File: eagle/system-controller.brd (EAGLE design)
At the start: 99 x 100 mm, 227 parts, among them IC1 TS4100, Q0 MOSFET-P-N-PAIR, Q1 MOSFET-P-N-PAIR, Q10 DNP/NTR4101P, Q11 DNP/NTR4101P, Q12 DNP/NTR4101P, Q2 MOSFET-P-N-PAIR, Q3 MOSFET-P-N-PAIR, Q4 MOSFET-P-N-PAIR, Q5 MOSFET-P-N-PAIR, Q6 MOSFET-P-N-PAIR, Q7 MOSFET-P-N-PAIR, Q9 DNP/NTR4101P, SW0 TPS25944LRVCRWQFN-20-3X4, SW1 TPS25944LRVCRWQFN-20-3X4, SW2 TPS25944LRVCRWQFN-20-3X4, SW3 TPS25944LRVCRWQFN-20-3X4, SW4 TPS25944LRVCRWQFN-20-3X4, SW5 TPS25944LRVCRWQFN-20-3X4, SW6 TPS25944LRVCRWQFN-20-3X4, SW7 TPS25944LRVCRWQFN-20-3X4, U1 MEGA128-A, X1 8 MHz CRYSTAL-ABRACON-ABM3-SMD

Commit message: latetest changes pushed
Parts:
- removed CFUSE7, RHWWD0, RHWWD1, RHWWD2: TBD, rcl_custom:.0603-B-NOSILK
- removed CFUSE7A: 1uF, rcl_custom:.0603-B-NOSILK
- removed LED12: DNP/AMB, psas_c3_team05:LED-0603
- removed RA8: 47k, rcl_custom:.0603-B-NOSILK
- removed RHWWD3: 1k, rcl_custom:.0603-B-NOSILK
- added C19: TBD, rcl_custom:.0603-B-NOSILK
- added C20: 1uF, rcl_custom:.0603-B-NOSILK
- added LED8: DNP/AMB, psas_c3_team05:LED-0603
- added RA0: 47k, rcl_custom:.0603-B-NOSILK
- added RN1, RN2, RN3: 390, rcl_custom:.0603-B-NOSILK
- added RN4: 10k, rcl_custom:.0603-B-NOSILK
- added TP28, TP29, TP30, TP31, TP32, TP33, TP34, TP5: TEST-POINT, Tova:2MM-TEST-POINT
- CN1: value TBD -> 22u
- J1: value (none) -> 1
- Q13: value (none) -> DON3035L
- RILIM0, RILIM1, RILIM2, RILIM3, RILIM4, RILIM5, RILIM6, RILIM7: value TBD -> 47k
- RNR: value TBD -> 470k
- moved R2 110.7 mm to (92.5, 88.7), turned to 0 degrees
- moved R8 106.5 mm to (92.5, 79.0), turned to 0 degrees
- moved R14 103.0 mm to (92.5, 69.5), turned to 0 degrees
- moved R20 99.5 mm to (92.5, 59.5), turned to 0 degrees
- moved R61 92.9 mm to (69.0, 5.50)
- moved R6 89.3 mm to (45.0, 5.50)
- moved R28 88.8 mm to (92.5, 49.5)
- moved R24 85.0 mm to (72.0, 5.50)
- moved R33 79.2 mm to (92.5, 39.4), turned to 0 degrees
- moved R12 78.9 mm to (47.9, 5.50)
- moved R22 78.2 mm to (75.0, 5.50)
- moved R23 73.6 mm to (78.0, 5.52)
- moved R38 73.5 mm to (92.5, 29.0), turned to 0 degrees
- moved R43 69.7 mm to (92.6, 18.9), turned to 0 degrees
- moved R18 69.4 mm to (51.0, 5.50)
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- renumbered CHWWD to CN1, RHWWD4 to RNR
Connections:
- net VBC1 renamed VCB1
- net VBC2 renamed VCB2
- net VBC4 renamed VCB4
- net VBC5 renamed VCB5
- net VBC6 renamed VCB6
- net VBC7 renamed VCB7
- removed net GMD: LED0.K
- net 3V: now also RA0.1; no longer RA8.1
- net GND: now also C19.2, C20.1, LED0.K, LED8.K, RN4.2; no longer CFUSE7.2, CFUSE7A.1, LED12.K, RHWWD3.2
- net I2C-SCL: now also TP5.1
- net I2C-SDA: now also TP28.1
- net N$109: now also RN1.1, RN2.1, RN3.1, RN4.1; no longer RHWWD0.1, RHWWD1.1, RHWWD2.1, RHWWD3.1
- net N$50: now also R2.2
- net N$53: now also LED11.A; no longer LED12.A
- net N$56: now also LED10.A; no longer LED11.A
- net N$57: now also LED8.A; no longer LED9.A
- net N$60: now also LED9.A; no longer LED10.A
- net N$70: now also C19.1; no longer CFUSE7.1
- net NUCLEAROPTION0: now also RN3.2; no longer RHWWD2.2
- net NUCLEAROPTION1: now also RN2.2; no longer RHWWD1.2
- net NUCLEAROPTION2: now also RN1.2; no longer RHWWD0.2
- net UART_FC_RX: now also TP30.1
- net UART_FC_TX: now also TP31.1
- net UART_FC_VCC: now also TP29.1
- net UART_LGR_RX: now also TP33.1
- net UART_LGR_TX: now also TP34.1
- net UART_LGR_VCC: now also TP32.1
- net VBUS: now also C20.2; no longer CFUSE7A.2
- net VCB0_!FLT: now also RA0.2; no longer RA1.2
- net VCB1_!FLT: now also RA1.2; no longer RA2.2
- net VCB2_!FLT: now also RA2.2; no longer RA3.2
- net VCB3_!FLT: now also RA3.2; no longer RA4.2
- net VCB4_!FLT: now also RA4.2; no longer RA5.2
- net VCB5_!FLT: now also RA5.2; no longer RA6.2
- net VCB6_!FLT: now also RA6.2; no longer RA7.2
- net VCB7_!FLT: now also RA7.2; no longer RA8.2
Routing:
- net VCB0_EN: track 14.2 -> 164.1 mm, vias 0 -> 4
- net VCB2_EN: track 15.8 -> 163.1 mm, vias 0 -> 4
- net N$55: track 2.19 -> 148.4 mm, vias 0 -> 2
- net VCB1_EN: track 14.9 -> 154.9 mm, vias 0 -> 6
- net N$49: track 145.1 -> 9.04 mm, vias 4 -> 0
- net VCB4_EN: track 16.1 -> 151.2 mm, vias 0 -> 6
- net N$63: track 140.8 -> 9.35 mm, vias 4 -> 0
- net N$57: track 128.5 -> 0.00 mm, vias 2 -> 0
- net N$95: track 134.8 -> 9.24 mm, vias 4 -> 0
- net N$58: track 2.16 -> 126.4 mm, vias 0 -> 2
- net N$60: track 118.3 -> 0.00 mm, vias 2 -> 0
- net PCB3_EN: track 16.7 -> 134.6 mm, vias 0 -> 4
- net N$61: track 2.16 -> 117.3 mm, vias 0 -> 2
- net N$26: track 114.8 -> 1.96 mm, vias 2 -> 0
- net N$87: track 118.8 -> 9.11 mm, vias 4 -> 0
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- added copper zone on layer 1, net V+
- added copper zone on layer 1, net VBUS
- added copper zone on layer 1, net VCB0
- added copper zone on layer 1, net VCB1
- added copper zone on layer 1, net VCB2
- added copper zone on layer 1, net VCB3
- added copper zone on layer 1, net VCB4
- added copper zone on layer 1, net VCB5
- added copper zone on layer 1, net VCB6
- added copper zone on layer 1, net VCB7
- added copper zone on layer 1, net VSOL

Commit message: latest changes... thicker polys, moved some traces, more...
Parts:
- moved TP28 53.8 mm to (30.1, 86.6)
- moved TP5 42.6 mm to (33.2, 86.6)
- moved TP0GHT 3.25 mm to (87.5, 89.3)
- moved C12 2.40 mm to (81.9, 41.2)
- moved CFUSE3A 2.40 mm to (82.0, 51.3)
- moved TP1GHT 2.40 mm to (85.9, 68.9)
- moved TP1GOOD 2.40 mm to (83.4, 78.0)
- moved TP2GOOD 2.40 mm to (83.4, 68.9)
- moved TP3GHT 2.40 mm to (86.2, 48.5)
- moved TP3GOOD 2.40 mm to (83.4, 58.9)
- moved TP4GHT 2.40 mm to (86.2, 38.2)
- moved TP4GOOD 2.40 mm to (83.5, 48.5)
- moved TP5GHT 2.40 mm to (86.2, 28.0)
- moved TP5GOOD 2.40 mm to (83.5, 38.2)
- moved TP6GHT 2.40 mm to (86.2, 18.0)
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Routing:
- net N$61: track 117.3 -> 148.5 mm, vias 2 -> 8
- net GND: track 0.00 -> 30.9 mm, vias 0 -> 93
- net N$54: track 109.8 -> 125.6 mm, vias 2 -> 9
- net VBUS: track 38.1 -> 25.4 mm
- net VCB1_EN: track 154.9 -> 145.3 mm
- net N$55: track 148.4 -> 155.1 mm, vias 2 -> 4
- net I2C-SDA: track 92.9 -> 88.4 mm
- net N$15: track 65.0 -> 60.8 mm
- net TXD0: track 111.3 -> 107.2 mm
- net N$67: track 13.8 -> 10.3 mm
- net N$83: track 13.6 -> 10.2 mm
- net N$99: track 13.5 -> 10.2 mm
- net N$91: track 13.4 -> 10.3 mm
- net N$75: track 13.5 -> 10.3 mm
- net VCB0: track 115.4 -> 112.4 mm
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
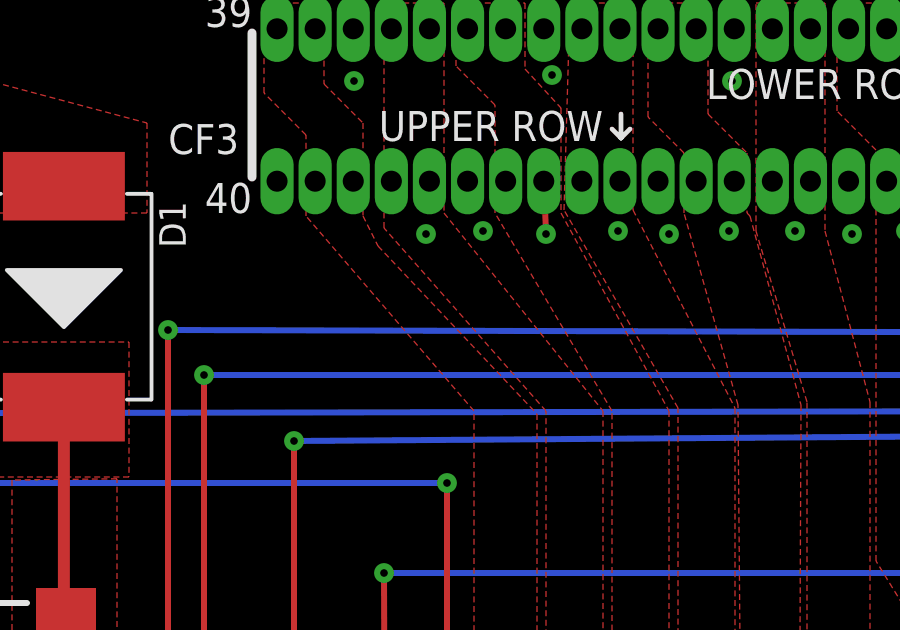
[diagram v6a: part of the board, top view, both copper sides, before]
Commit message: added the RIMON resister value and dV/dt cap value
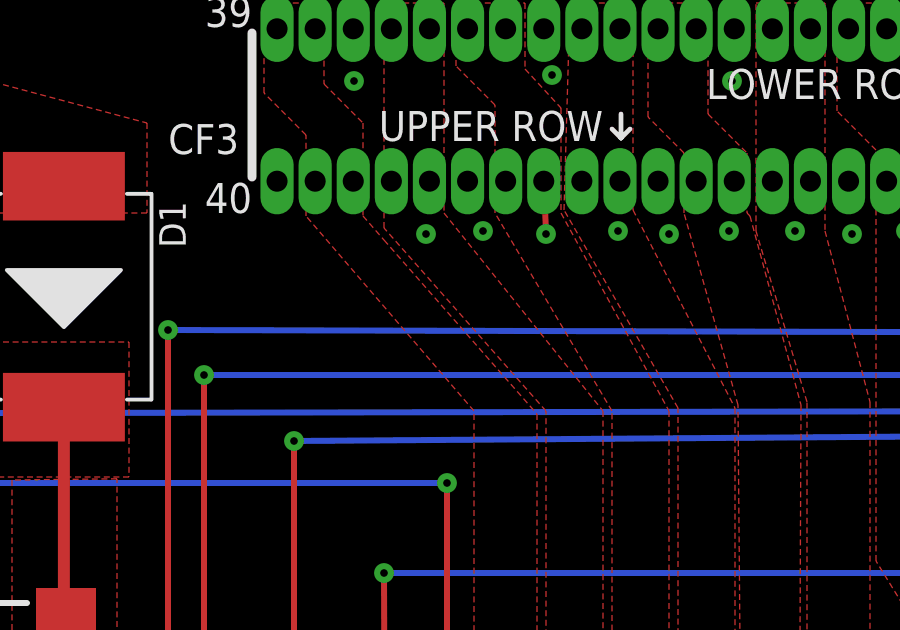
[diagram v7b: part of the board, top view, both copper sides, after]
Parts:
- C11, C13, C15, C17, C19, C3, C5, C9: value TBD -> 2.2nF
- RIMON0, RIMON1, RIMON2, RIMON3, RIMON4, RIMON5, RIMON6, RIMON7: value TBD -> 4.7k
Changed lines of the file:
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@@
 <attribute name="MPN" value="Texas Instruments" x="82.1" y="84.1" size="1.778" layer="27" rot="R180" display="off"/>
 </element>
-<element name="RIMON0" library="rcl_custom" package=".0603-B-NOSILK" value="TBD" x="43" y="61" rot="R90"/>
-<element name="C3" library="rcl_custom" package=".0603-B-NOSILK" value="TBD" x="87.5" y="85" smashed="yes" rot="R90">
+<element name="RIMON0" library="rcl_custom" package=".0603-B-NOSILK" value="4.7k" x="43" y="61" rot="R90"/>
+<element name="C3" library="rcl_custom" package=".0603-B-NOSILK" value="2.2nF" x="87.5" y="85" smashed="yes" rot="R90">
 <attribute name="NAME" x="88.2" y="79.3" size="0.8" layer="25" font="vector" ratio="15" rot="R90"/>
 <attribute name="VALUE" x="89.1" y="83.8" size="0.8" layer="27" font="vector" ratio="15" rot="R90"/>
@@
 </element>
 <element name="SW1" library="WQFN-20-3x4" package="QFN-20-L" value="TPS25944LRVCRWQFN-20-3X4" x="82.1" y="74.6" rot="R180"/>
-<element name="RIMON1" library="rcl_custom" package=".0603-B-NOSILK" value="TBD" x="40" y="61" rot="R90"/>
-<element name="C5" library="rcl_custom" package=".0603-B-NOSILK" value="TBD" x="87.5" y="75.5" smashed="yes" rot="R90">
+<element name="RIMON1" library="rcl_custom" package=".0603-B-NOSILK" value="4.7k" x="40" y="61" rot="R90"/>
+<element name="C5" library="rcl_custom" package=".0603-B-NOSILK" value="2.2nF" x="87.5" y="75.5" smashed="yes" rot="R90">
 <attribute name="NAME" x="87.7" y="76.3" size="0.8" layer="25" font="vector" ratio="15" rot="R90"/>
 <attribute name="VALUE" x="89.1" y="74.3" size="0.8" layer="27" font="vector" ratio="15" rot="R90"/>
@@
 </element>
 <element name="SW2" library="WQFN-20-3x4" package="QFN-20-L" value="TPS25944LRVCRWQFN-20-3X4" x="82.1" y="65.1" rot="R180"/>
-<element name="RIMON2" library="rcl_custom" package=".0603-B-NOSILK" value="TBD" x="37.1" y="61" smashed="yes" rot="R90">
+<element name="RIMON2" library="rcl_custom" package=".0603-B-NOSILK" value="4.7k" x="37.1" y="61" smashed="yes" rot="R90">
 <attribute name="NAME" x="36.3" y="59.8" size="0.8" layer="25" font="vector" ratio="15" rot="R90"/>
 <attribute name="VALUE" x="38.7" y="59.8" size="0.8" layer="27" font="vector" ratio="15" rot="R90"/>
 <attribute name="NAME" x="37.1" y="61" size="0.3" layer="33" ratio="15" rot="R90" align="center"/>
 </element>
-<element name="C9" library="rcl_custom" package=".0603-B-NOSILK" value="TBD" x="87.5" y="66" smashed="yes" rot="R90">
+<element name="C9" library="rcl_custom" package=".0603-B-NOSILK" value="2.2nF" x="87.5" y="66" smashed="yes" rot="R90">
 <attribute name="NAME" x="87.7" y="64.8" size="0.8" layer="25" font="vector" ratio="15" rot="R90"/>
 <attribute name="VALUE" x="89.1" y="64.8" size="0.8" layer="27" font="vector" ratio="15" rot="R90"/>
@@
 </element>
 <element name="SW7" library="WQFN-20-3x4" package="QFN-20-L" value="TPS25944LRVCRWQFN-20-3X4" x="82.1" y="14.6" rot="R180"/>
-<element name="RIMON7" library="rcl_custom" package=".0603-B-NOSILK" value="TBD" x="40.5" y="51" rot="R270"/>
-<element name="C19" library="rcl_custom" package=".0603-B-NOSILK" value="TBD" x="87.6" y="15.5" rot="R90"/>
+<element name="RIMON7" library="rcl_custom" package=".0603-B-NOSILK" value="4.7k" x="40.5" y="51" rot="R270"/>
+<element name="C19" library="rcl_custom" package=".0603-B-NOSILK" value="2.2nF" x="87.6" y="15.5" rot="R90"/>
 <element name="SW5" library="WQFN-20-3x4" package="QFN-20-L" value="TPS25944LRVCRWQFN-20-3X4" x="82.1" y="35.1" rot="R180"/>
-<element name="RIMON5" library="rcl_custom" package=".0603-B-NOSILK" value="TBD" x="42.17" y="50.99" rot="R270"/>
-<element name="C15" library="rcl_custom" package=".0603-B-NOSILK" value="TBD" x="87.5" y="35.9" rot="R90"/>
+<element name="RIMON5" library="rcl_custom" package=".0603-B-NOSILK" value="4.7k" x="42.17" y="50.99" rot="R270"/>
+<element name="C15" library="rcl_custom" package=".0603-B-NOSILK" value="2.2nF" x="87.5" y="35.9" rot="R90"/>
 <element name="SW4" library="WQFN-20-3x4" package="QFN-20-L" value="TPS25944LRVCRWQFN-20-3X4" x="82.1" y="45.1" rot="R180"/>
-<element name="RIMON4" library="rcl_custom" package=".0603-B-NOSILK" value="TBD" x="36" y="55" rot="R180"/>
-<element name="C13" library="rcl_custom" package=".0603-B-NOSILK" value="TBD" x="87.5" y="46" smashed="yes" rot="R90">
+<element name="RIMON4" library="rcl_custom" package=".0603-B-NOSILK" value="4.7k" x="36" y="55" rot="R180"/>
+<element name="C13" library="rcl_custom" package=".0603-B-NOSILK" value="2.2nF" x="87.5" y="46" smashed="yes" rot="R90">
 <attribute name="NAME" x="88.7" y="32.3" size="0.8" layer="25" font="vector" ratio="15" rot="R90"/>
 <attribute name="VALUE" x="89.1" y="44.8" size="0.8" layer="27" font="vector" ratio="15" rot="R90"/>
@@
 </element>
 <element name="SW3" library="WQFN-20-3x4" package="QFN-20-L" value="TPS25944LRVCRWQFN-20-3X4" x="82.1" y="55.1" rot="R180"/>
-<element name="RIMON3" library="rcl_custom" package=".0603-B-NOSILK" value="TBD" x="46" y="61" rot="R90"/>
-<element name="C11" library="rcl_custom" package=".0603-B-NOSILK" value="TBD" x="87.5" y="56" smashed="yes" rot="R90">
+<element name="RIMON3" library="rcl_custom" package=".0603-B-NOSILK" value="4.7k" x="46" y="61" rot="R90"/>
+<element name="C11" library="rcl_custom" package=".0603-B-NOSILK" value="2.2nF" x="87.5" y="56" smashed="yes" rot="R90">
 <attribute name="NAME" x="88.2" y="52.3" size="0.8" layer="25" font="vector" ratio="15" rot="R90"/>
 <attribute name="VALUE" x="89.1" y="54.8" size="0.8" layer="27" font="vector" ratio="15" rot="R90"/>
@@
 </element>
 <element name="SW6" library="WQFN-20-3x4" package="QFN-20-L" value="TPS25944LRVCRWQFN-20-3X4" x="82.1" y="24.6" rot="R180"/>
-<element name="RIMON6" library="rcl_custom" package=".0603-B-NOSILK" value="TBD" x="36" y="53" rot="R180"/>
-<element name="C17" library="rcl_custom" package=".0603-B-NOSILK" value="TBD" x="87.51" y="25.5" rot="R89.8"/>
+<element name="RIMON6" library="rcl_custom" package=".0603-B-NOSILK" value="4.7k" x="36" y="53" rot="R180"/>
+<element name="C17" library="rcl_custom" package=".0603-B-NOSILK" value="2.2nF" x="87.51" y="25.5" rot="R89.8"/>
 <element name="RA5" library="rcl_custom" package=".0603-B-NOSILK" value="47k" x="8.3" y="35.5">
 <attribute name="DIST" value="digikey" x="8.3" y="35.5" size="1.778" layer="27" display="off"/>
@@
 <vertex x="60.3" y="95"/>
 <vertex x="60.3" y="91.9"/>
-<vertex x="60.8" y="90.9"/>
+<vertex x="61" y="91.1"/>
 <vertex x="66.1" y="85.3"/>
 <vertex x="66.1" y="27.9"/>

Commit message: latest minor changes
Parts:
- RIMON0, RIMON1, RIMON2, RIMON3, RIMON4, RIMON5, RIMON6, RIMON7: value 4.7k -> 47k
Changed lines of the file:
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@@
 <attribute name="MPN" value="Texas Instruments" x="82.1" y="84.1" size="1.778" layer="27" rot="R180" display="off"/>
 </element>
-<element name="RIMON0" library="rcl_custom" package=".0603-B-NOSILK" value="4.7k" x="43" y="61" rot="R90"/>
+<element name="RIMON0" library="rcl_custom" package=".0603-B-NOSILK" value="47k" x="43" y="61" rot="R90"/>
 <element name="C3" library="rcl_custom" package=".0603-B-NOSILK" value="2.2nF" x="87.5" y="85" smashed="yes" rot="R90">
 <attribute name="NAME" x="88.2" y="79.3" size="0.8" layer="25" font="vector" ratio="15" rot="R90"/>
@@
 </element>
 <element name="SW1" library="WQFN-20-3x4" package="QFN-20-L" value="TPS25944LRVCRWQFN-20-3X4" x="82.1" y="74.6" rot="R180"/>
-<element name="RIMON1" library="rcl_custom" package=".0603-B-NOSILK" value="4.7k" x="40" y="61" rot="R90"/>
+<element name="RIMON1" library="rcl_custom" package=".0603-B-NOSILK" value="47k" x="40" y="61" rot="R90"/>
 <element name="C5" library="rcl_custom" package=".0603-B-NOSILK" value="2.2nF" x="87.5" y="75.5" smashed="yes" rot="R90">
 <attribute name="NAME" x="87.7" y="76.3" size="0.8" layer="25" font="vector" ratio="15" rot="R90"/>
@@
 </element>
 <element name="SW2" library="WQFN-20-3x4" package="QFN-20-L" value="TPS25944LRVCRWQFN-20-3X4" x="82.1" y="65.1" rot="R180"/>
-<element name="RIMON2" library="rcl_custom" package=".0603-B-NOSILK" value="4.7k" x="37.1" y="61" smashed="yes" rot="R90">
+<element name="RIMON2" library="rcl_custom" package=".0603-B-NOSILK" value="47k" x="37.1" y="61" smashed="yes" rot="R90">
 <attribute name="NAME" x="36.3" y="59.8" size="0.8" layer="25" font="vector" ratio="15" rot="R90"/>
 <attribute name="VALUE" x="38.7" y="59.8" size="0.8" layer="27" font="vector" ratio="15" rot="R90"/>
@@
 </element>
 <element name="SW7" library="WQFN-20-3x4" package="QFN-20-L" value="TPS25944LRVCRWQFN-20-3X4" x="82.1" y="14.6" rot="R180"/>
-<element name="RIMON7" library="rcl_custom" package=".0603-B-NOSILK" value="4.7k" x="40.5" y="51" rot="R270"/>
+<element name="RIMON7" library="rcl_custom" package=".0603-B-NOSILK" value="47k" x="40.5" y="51" rot="R270"/>
 <element name="C19" library="rcl_custom" package=".0603-B-NOSILK" value="2.2nF" x="87.6" y="15.5" rot="R90"/>
 <element name="SW5" library="WQFN-20-3x4" package="QFN-20-L" value="TPS25944LRVCRWQFN-20-3X4" x="82.1" y="35.1" rot="R180"/>
-<element name="RIMON5" library="rcl_custom" package=".0603-B-NOSILK" value="4.7k" x="42.17" y="50.99" rot="R270"/>
+<element name="RIMON5" library="rcl_custom" package=".0603-B-NOSILK" value="47k" x="42.17" y="50.99" rot="R270"/>
 <element name="C15" library="rcl_custom" package=".0603-B-NOSILK" value="2.2nF" x="87.5" y="35.9" rot="R90"/>
 <element name="SW4" library="WQFN-20-3x4" package="QFN-20-L" value="TPS25944LRVCRWQFN-20-3X4" x="82.1" y="45.1" rot="R180"/>
-<element name="RIMON4" library="rcl_custom" package=".0603-B-NOSILK" value="4.7k" x="36" y="55" rot="R180"/>
+<element name="RIMON4" library="rcl_custom" package=".0603-B-NOSILK" value="47k" x="36" y="55" rot="R180"/>
 <element name="C13" library="rcl_custom" package=".0603-B-NOSILK" value="2.2nF" x="87.5" y="46" smashed="yes" rot="R90">
 <attribute name="NAME" x="88.7" y="32.3" size="0.8" layer="25" font="vector" ratio="15" rot="R90"/>
@@
 </element>
 <element name="SW3" library="WQFN-20-3x4" package="QFN-20-L" value="TPS25944LRVCRWQFN-20-3X4" x="82.1" y="55.1" rot="R180"/>
-<element name="RIMON3" library="rcl_custom" package=".0603-B-NOSILK" value="4.7k" x="46" y="61" rot="R90"/>
+<element name="RIMON3" library="rcl_custom" package=".0603-B-NOSILK" value="47k" x="46" y="61" rot="R90"/>
 <element name="C11" library="rcl_custom" package=".0603-B-NOSILK" value="2.2nF" x="87.5" y="56" smashed="yes" rot="R90">
 <attribute name="NAME" x="88.2" y="52.3" size="0.8" layer="25" font="vector" ratio="15" rot="R90"/>
@@
 </element>
 <element name="SW6" library="WQFN-20-3x4" package="QFN-20-L" value="TPS25944LRVCRWQFN-20-3X4" x="82.1" y="24.6" rot="R180"/>
-<element name="RIMON6" library="rcl_custom" package=".0603-B-NOSILK" value="4.7k" x="36" y="53" rot="R180"/>
+<element name="RIMON6" library="rcl_custom" package=".0603-B-NOSILK" value="47k" x="36" y="53" rot="R180"/>
 <element name="C17" library="rcl_custom" package=".0603-B-NOSILK" value="2.2nF" x="87.51" y="25.5" rot="R89.8"/>
 <element name="RA5" library="rcl_custom" package=".0603-B-NOSILK" value="47k" x="8.3" y="35.5">
